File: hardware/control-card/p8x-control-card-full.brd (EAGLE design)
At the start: 160 x 100 mm, 58 parts, among them J1 FABC96R, U1 74HCT161, U10 28C64, U11 28C64, U12 28C64, U13 28C64, U14 74HCT374, U15 74HCT374, U16 74HCT374, U17 74HCT374, U18 74HCT161, U19 74HCT86, U2 74HCT14, U20 74HCT244, U21 74HCT74, U3 74HCT74, U4 74HCT00, U5 74HCT08, U6 74HCT32, U7 74HCT377, U8 74HCT138, U9 74HCT151, X1 4MHZ

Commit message: feat(hardware): use con-vg DIN 41612 footprints (MABC96R card / FABC96S backplane)
Replace the hand-rolled DIN96/DIN96C connector packages with the real Eagle
con-vg DIN 41612 footprints (geometry baked into the generator so it stays
self-contained): card edge = MABC96R (male right-angle), backplane = FABC96S
(female vertical) — both A/B/C @ 2.54mm, drill 0.9144, two M2.5 mounting holes
at y=+/-45. Card value -> MABC96R; pin->pad names unchanged (A1..C32) so the
netlist is intact.

con-vg centres the pad field on the element origin, so the backplane (hand-
placed/routed) was re-derived: slots dropped to y=54.6 to centre the pin field
on the 109mm board (pads now on-board), bus traces re-routed to the new A/B/C
columns (element at sx(i)-2.54). Cards auto-adapt via fp_box. All 8 boards
validate (0 errors).

Known: 3 placement-overlap WARNINGS on the backplane (power-LED resistor; CT2/RT1
clock terminators, both DNP) where the taller connector crowds the top/bottom
strips — to clear during the Fusion placement pass.

Co-Authored-By: Claude Opus 4.8 <noreply@anthropic.com>
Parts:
- J1: value FABC96R -> MABC96R; device p8x:DIN96C -> p8x:MABC96R
- moved J1 37.5 mm to (7.94, 49.6)

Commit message: feat(hardware): 100nF bypass caps to 0.1" lead pitch on all boards
The 100nF ceramic-disc decoupling/bypass caps used the shared C_DISC footprint
at 0.2" (5.08mm) lead spacing. The parts being sourced are 0.1" (2.54mm) pitch,
so retarget just those caps:

- Add a C_DISC1 footprint (pad 2 at y=-2.54) and a CAP1 device that reuses the
  CAP schematic symbol art but points at C_DISC1.
- Route the 100nF parts to CAP1: per-IC decoupling (CDn), the placement-flow
  copies, and the backplane per-slot caps C1-C10.
- Leave C_DISC (0.2") for the parts that still use it: the 1uF caps, the 150pF
  clock terminators (CT1/CT2), and the XTAL32 placeholder.

Regenerated all 8 boards (.sch/.brd/-full.brd) and the schematic PDFs; the
narrower pad field also relieves the backplane connector clearance. Validation:
0 errors on all boards.

Co-Authored-By: Claude Opus 4.8 <noreply@anthropic.com>
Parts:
- CD1, CD10, CD11, CD12, CD13, CD14, CD15, CD16, CD17, CD18, CD19, CD2, CD20, CD21, CD3, CD4, CD5, CD6, CD7, CD8, CD9: device p8x:C_DISC -> p8x:C_DISC1
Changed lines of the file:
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@@
 <attribute name="VALUE" x="17.87" y="92.66" size="1.778" layer="27" ratio="10"/>
 </element>
-<element name="CD1" library="p8x" package="C_DISC" value="100N" x="29.79" y="95.10" smashed="yes">
+<element name="CD1" library="p8x" package="C_DISC1" value="100N" x="29.79" y="95.10" smashed="yes">
 <attribute name="NAME" x="29.79" y="97.64" size="1.778" layer="25" ratio="10"/>
 <attribute name="VALUE" x="29.79" y="92.56" size="1.778" layer="27" ratio="10"/>
@@
 <attribute name="VALUE" x="34.09" y="92.66" size="1.778" layer="27" ratio="10"/>
 </element>
-<element name="CD2" library="p8x" package="C_DISC" value="100N" x="46.01" y="95.10" smashed="yes">
+<element name="CD2" library="p8x" package="C_DISC1" value="100N" x="46.01" y="95.10" smashed="yes">
 <attribute name="NAME" x="46.01" y="97.64" size="1.778" layer="25" ratio="10"/>
 <attribute name="VALUE" x="46.01" y="92.56" size="1.778" layer="27" ratio="10"/>
@@
 <attribute name="VALUE" x="50.31" y="92.66" size="1.778" layer="27" ratio="10"/>
 </element>
-<element name="CD3" library="p8x" package="C_DISC" value="100N" x="62.23" y="95.10" smashed="yes">
+<element name="CD3" library="p8x" package="C_DISC1" value="100N" x="62.23" y="95.10" smashed="yes">
 <attribute name="NAME" x="62.23" y="97.64" size="1.778" layer="25" ratio="10"/>
 <attribute name="VALUE" x="62.23" y="92.56" size="1.778" layer="27" ratio="10"/>
@@
 <attribute name="VALUE" x="66.53" y="92.66" size="1.778" layer="27" ratio="10"/>
 </element>
-<element name="CD4" library="p8x" package="C_DISC" value="100N" x="78.45" y="95.10" smashed="yes">
+<element name="CD4" library="p8x" package="C_DISC1" value="100N" x="78.45" y="95.10" smashed="yes">
 <attribute name="NAME" x="78.45" y="97.64" size="1.778" layer="25" ratio="10"/>
 <attribute name="VALUE" x="78.45" y="92.56" size="1.778" layer="27" ratio="10"/>
@@
 <attribute name="VALUE" x="82.75" y="92.66" size="1.778" layer="27" ratio="10"/>
 </element>
-<element name="CD5" library="p8x" package="C_DISC" value="100N" x="94.67" y="95.10" smashed="yes">
+<element name="CD5" library="p8x" package="C_DISC1" value="100N" x="94.67" y="95.10" smashed="yes">
 <attribute name="NAME" x="94.67" y="97.64" size="1.778" layer="25" ratio="10"/>
 <attribute name="VALUE" x="94.67" y="92.56" size="1.778" layer="27" ratio="10"/>
@@
 <attribute name="VALUE" x="98.97" y="92.66" size="1.778" layer="27" ratio="10"/>
 </element>
-<element name="CD6" library="p8x" package="C_DISC" value="100N" x="110.89" y="95.10" smashed="yes">
+<element name="CD6" library="p8x" package="C_DISC1" value="100N" x="110.89" y="95.10" smashed="yes">
 <attribute name="NAME" x="110.89" y="97.64" size="1.778" layer="25" ratio="10"/>
 <attribute name="VALUE" x="110.89" y="92.56" size="1.778" layer="27" ratio="10"/>
@@
 <attribute name="VALUE" x="115.19" y="92.66" size="1.778" layer="27" ratio="10"/>
 </element>
-<element name="CD7" library="p8x" package="C_DISC" value="100N" x="127.11" y="95.10" smashed="yes">
+<element name="CD7" library="p8x" package="C_DISC1" value="100N" x="127.11" y="95.10" smashed="yes">
 <attribute name="NAME" x="127.11" y="97.64" size="1.778" layer="25" ratio="10"/>
 <attribute name="VALUE" x="127.11" y="92.56" size="1.778" layer="27" ratio="10"/>
@@
 <attribute name="VALUE" x="131.41" y="92.66" size="1.778" layer="27" ratio="10"/>
 </element>
-<element name="CD8" library="p8x" package="C_DISC" value="100N" x="143.33" y="95.10" smashed="yes">
+<element name="CD8" library="p8x" package="C_DISC1" value="100N" x="143.33" y="95.10" smashed="yes">
 <attribute name="NAME" x="143.33" y="97.64" size="1.778" layer="25" ratio="10"/>
 <attribute name="VALUE" x="143.33" y="92.56" size="1.778" layer="27" ratio="10"/>
@@
 <attribute name="VALUE" x="17.87" y="65.60" size="1.778" layer="27" ratio="10"/>
 </element>
-<element name="CD9" library="p8x" package="C_DISC" value="100N" x="29.79" y="68.04" smashed="yes">
+<element name="CD9" library="p8x" package="C_DISC1" value="100N" x="29.79" y="68.04" smashed="yes">
 <attribute name="NAME" x="29.79" y="70.58" size="1.778" layer="25" ratio="10"/>
 <attribute name="VALUE" x="29.79" y="65.50" size="1.778" layer="27" ratio="10"/>
@@
 <attribute name="VALUE" x="34.09" y="65.60" size="1.778" layer="27" ratio="10"/>
 </element>
-<element name="CD10" library="p8x" package="C_DISC" value="100N" x="53.63" y="68.04" smashed="yes">
+<element name="CD10" library="p8x" package="C_DISC1" value="100N" x="53.63" y="68.04" smashed="yes">
 <attribute name="NAME" x="53.63" y="70.58" size="1.778" layer="25" ratio="10"/>
 <attribute name="VALUE" x="53.63" y="65.50" size="1.778" layer="27" ratio="10"/>
@@
 <attribute name="VALUE" x="57.93" y="65.60" size="1.778" layer="27" ratio="10"/>
 </element>
-<element name="CD11" library="p8x" package="C_DISC" value="100N" x="77.47" y="68.04" smashed="yes">
+<element name="CD11" library="p8x" package="C_DISC1" value="100N" x="77.47" y="68.04" smashed="yes">
 <attribute name="NAME" x="77.47" y="70.58" size="1.778" layer="25" ratio="10"/>
 <attribute name="VALUE" x="77.47" y="65.50" size="1.778" layer="27" ratio="10"/>
@@
 <attribute name="VALUE" x="81.77" y="65.60" size="1.778" layer="27" ratio="10"/>
 </element>
-<element name="CD12" library="p8x" package="C_DISC" value="100N" x="101.31" y="68.04" smashed="yes">
+<element name="CD12" library="p8x" package="C_DISC1" value="100N" x="101.31" y="68.04" smashed="yes">
 <attribute name="NAME" x="101.31" y="70.58" size="1.778" layer="25" ratio="10"/>
 <attribute name="VALUE" x="101.31" y="65.50" size="1.778" layer="27" ratio="10"/>
@@
 <attribute name="VALUE" x="105.61" y="65.60" size="1.778" layer="27" ratio="10"/>
 </element>
-<element name="CD13" library="p8x" package="C_DISC" value="100N" x="125.15" y="68.04" smashed="yes">
+<element name="CD13" library="p8x" package="C_DISC1" value="100N" x="125.15" y="68.04" smashed="yes">
 <attribute name="NAME" x="125.15" y="70.58" size="1.778" layer="25" ratio="10"/>
 <attribute name="VALUE" x="125.15" y="65.50" size="1.778" layer="27" ratio="10"/>
@@
 <attribute name="VALUE" x="129.45" y="65.60" size="1.778" layer="27" ratio="10"/>
 </element>
-<element name="CD14" library="p8x" package="C_DISC" value="100N" x="141.37" y="68.04" smashed="yes">
+<element name="CD14" library="p8x" package="C_DISC1" value="100N" x="141.37" y="68.04" smashed="yes">
 <attribute name="NAME" x="141.37" y="70.58" size="1.778" layer="25" ratio="10"/>
 <attribute name="VALUE" x="141.37" y="65.50" size="1.778" layer="27" ratio="10"/>
@@
 <attribute name="VALUE" x="145.67" y="65.60" size="1.778" layer="27" ratio="10"/>
 </element>
-<element name="CD15" library="p8x" package="C_DISC" value="100N" x="17.97" y="30.82" smashed="yes">
+<element name="CD15" library="p8x" package="C_DISC1" value="100N" x="17.97" y="30.82" smashed="yes">
 <attribute name="NAME" x="17.97" y="33.36" size="1.778" layer="25" ratio="10"/>
 <attribute name="VALUE" x="17.97" y="28.28" size="1.778" layer="27" ratio="10"/>
@@
 <attribute name="VALUE" x="22.27" y="28.38" size="1.778" layer="27" ratio="10"/>
 </element>
-<element name="CD16" library="p8x" package="C_DISC" value="100N" x="34.19" y="30.82" smashed="yes">
+<element name="CD16" library="p8x" package="C_DISC1" value="100N" x="34.19" y="30.82" smashed="yes">
 <attribute name="NAME" x="34.19" y="33.36" size="1.778" layer="25" ratio="10"/>
 <attribute name="VALUE" x="34.19" y="28.28" size="1.778" layer="27" ratio="10"/>
@@
 <attribute name="VALUE" x="38.49" y="28.38" size="1.778" layer="27" ratio="10"/>
 </element>
-<element name="CD17" library="p8x" package="C_DISC" value="100N" x="50.41" y="30.82" smashed="yes">
+<element name="CD17" library="p8x" package="C_DISC1" value="100N" x="50.41" y="30.82" smashed="yes">
 <attribute name="NAME" x="50.41" y="33.36" size="1.778" layer="25" ratio="10"/>
 <attribute name="VALUE" x="50.41" y="28.28" size="1.778" layer="27" ratio="10"/>
@@
 <attribute name="VALUE" x="54.71" y="28.38" size="1.778" layer="27" ratio="10"/>
 </element>
-<element name="CD18" library="p8x" package="C_DISC" value="100N" x="66.63" y="30.82" smashed="yes">
+<element name="CD18" library="p8x" package="C_DISC1" value="100N" x="66.63" y="30.82" smashed="yes">
 <attribute name="NAME" x="66.63" y="33.36" size="1.778" layer="25" ratio="10"/>
 <attribute name="VALUE" x="66.63" y="28.28" size="1.778" layer="27" ratio="10"/>
@@
 <attribute name="VALUE" x="70.93" y="28.38" size="1.778" layer="27" ratio="10"/>
 </element>
-<element name="CD19" library="p8x" package="C_DISC" value="100N" x="82.85" y="30.82" smashed="yes">
+<element name="CD19" library="p8x" package="C_DISC1" value="100N" x="82.85" y="30.82" smashed="yes">
 <attribute name="NAME" x="82.85" y="33.36" size="1.778" layer="25" ratio="10"/>
 <attribute name="VALUE" x="82.85" y="28.28" size="1.778" layer="27" ratio="10"/>
@@
 <attribute name="VALUE" x="87.15" y="28.38" size="1.778" layer="27" ratio="10"/>
 </element>
-<element name="CD20" library="p8x" package="C_DISC" value="100N" x="99.07" y="30.82" smashed="yes">
+<element name="CD20" library="p8x" package="C_DISC1" value="100N" x="99.07" y="30.82" smashed="yes">
 <attribute name="NAME" x="99.07" y="33.36" size="1.778" layer="25" ratio="10"/>
 <attribute name="VALUE" x="99.07" y="28.28" size="1.778" layer="27" ratio="10"/>
@@
 <attribute name="VALUE" x="103.37" y="28.38" size="1.778" layer="27" ratio="10"/>
 </element>
-<element name="CD21" library="p8x" package="C_DISC" value="100N" x="115.29" y="30.82" smashed="yes">
+<element name="CD21" library="p8x" package="C_DISC1" value="100N" x="115.29" y="30.82" smashed="yes">
 <attribute name="NAME" x="115.29" y="33.36" size="1.778" layer="25" ratio="10"/>
 <attribute name="VALUE" x="115.29" y="28.28" size="1.778" layer="27" ratio="10"/>

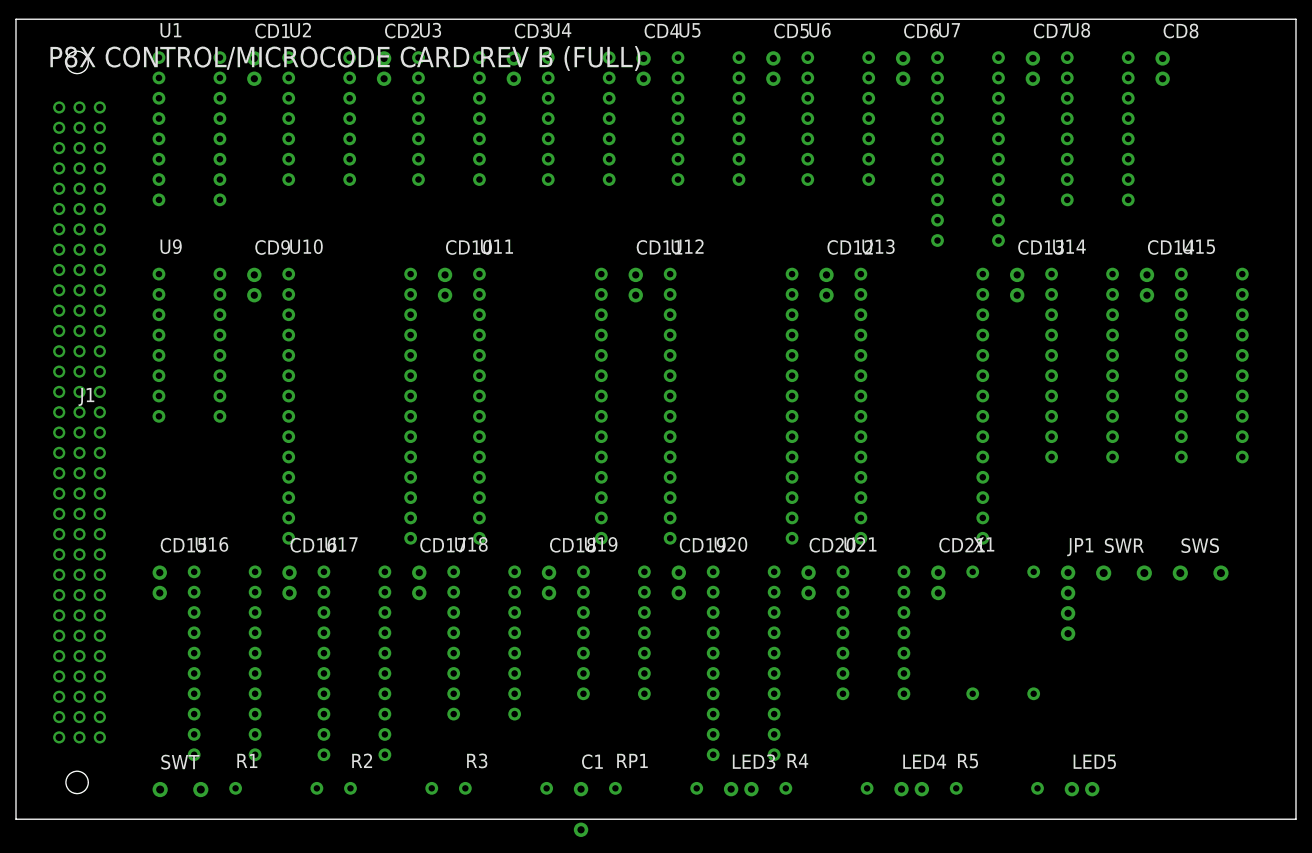
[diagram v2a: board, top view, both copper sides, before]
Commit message: hardware: silkscreen off footprints, standard cap value format, backplane RL1->R1
Pre-Fusion cleanup so there is less to fix by hand once placing/routing.

1. SILKSCREEN NO LONGER OVERLAYS FOOTPRINTS (all boards). NAME/VALUE were emitted
   at the element origin +/-2.54 regardless of part size, so on anything bigger
   than a 2-pin part the text landed ON the pads -- the 96-pin DIN connector had
   J1/SLOT1 across its pad field, and caps had their values on top of them. Now
   placed against the real footprint bbox (fp_box): NAME 0.7mm above the top edge,
   VALUE 0.7mm below the bottom, left-aligned to the box. Verified: 1642
   silkscreen labels across all 9 boards, 0 sitting on a footprint (was many).
   Not rotation-aware, which is fine -- no board rotates a part today.

2. CAPACITOR VALUES use standard unit suffixes: 100N->100nF, 470U->470uF,
   150P->150pF, 1U->1uF (and the DNP/x10 variants). Applied everywhere, so the
   per-IC decoupling caps on every card change too. No doc quoted the raw value
   strings, so no doc churn.

3. BACKPLANE RL1 -> R1 (standard R designator). Scoped to the backplane section
   only -- the io-card and led-card have their own unrelated RL1 (8x330R networks)
   which are untouched. Backplane theory/design docs updated to match.

Part refs/values are decided in gen_eagle.py: the backplane `small=[...]` list and
each cards `ic`/`sm` dicts.

Co-Authored-By: Claude Opus 4.8 <noreply@anthropic.com>
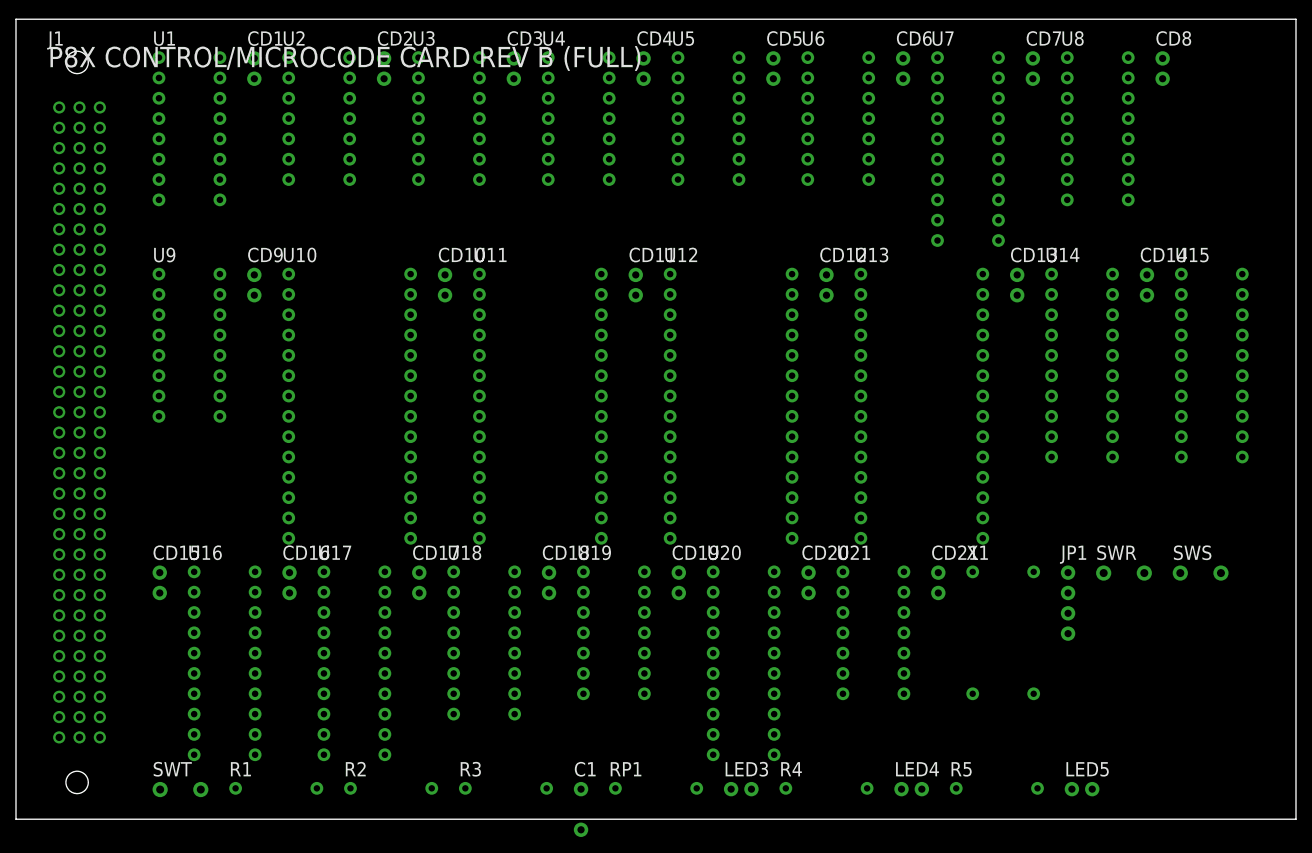
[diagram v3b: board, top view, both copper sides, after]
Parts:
- C1: value 1U -> 1uF
- CD1, CD10, CD11, CD12, CD13, CD14, CD15, CD16, CD17, CD18, CD19, CD2, CD20, CD21, CD3, CD4, CD5, CD6, CD7, CD8, CD9: value 100N -> 100nF
